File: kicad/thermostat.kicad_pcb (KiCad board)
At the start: 2 copper layers, 108 x 80 mm, 27 parts, among them IC1 LM2596S-5, J1 Display i2c, J2 Sensor i2c, J6 Screw_Terminal_01x05

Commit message: Updates for v1.1
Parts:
- L1: footprint Inductors_SMD:L_Wuerth_WE-PD-Typ-LS -> Inductors_SMD:L_Wuerth_WE-PD-Typ-M-Typ-S
- moved L1 3.50 mm to (167.8, 163.5)
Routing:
- net Net-(D2-Pad1): track 57.7 -> 55.9 mm

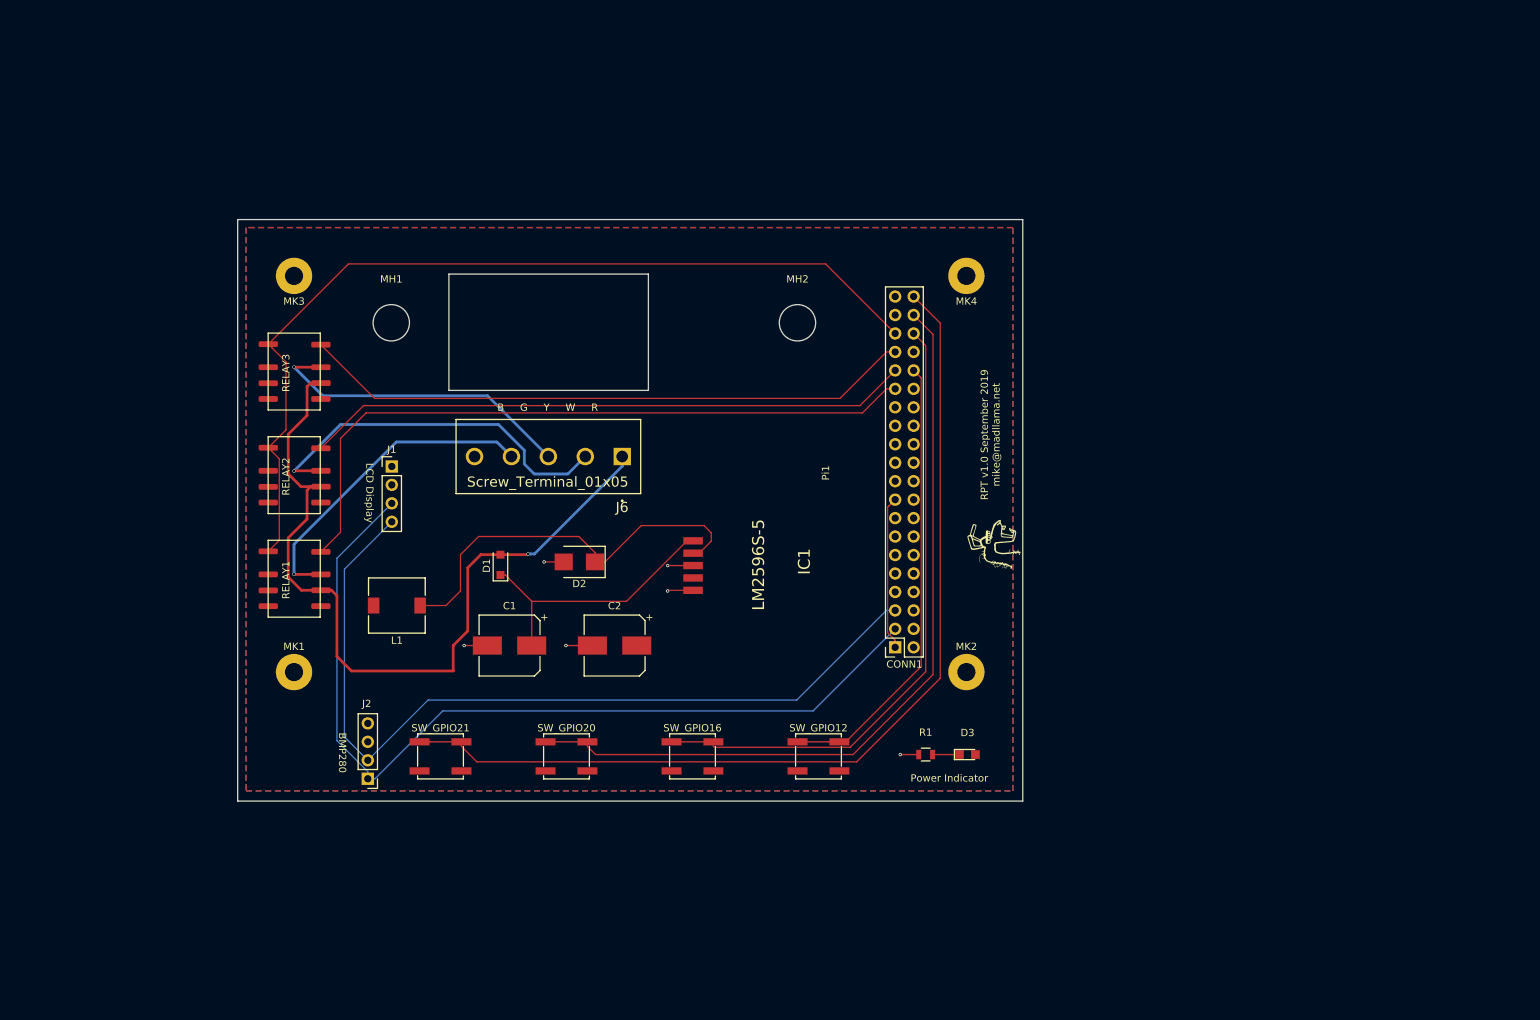
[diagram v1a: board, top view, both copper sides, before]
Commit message: Support for KiCad v5.14 libraries
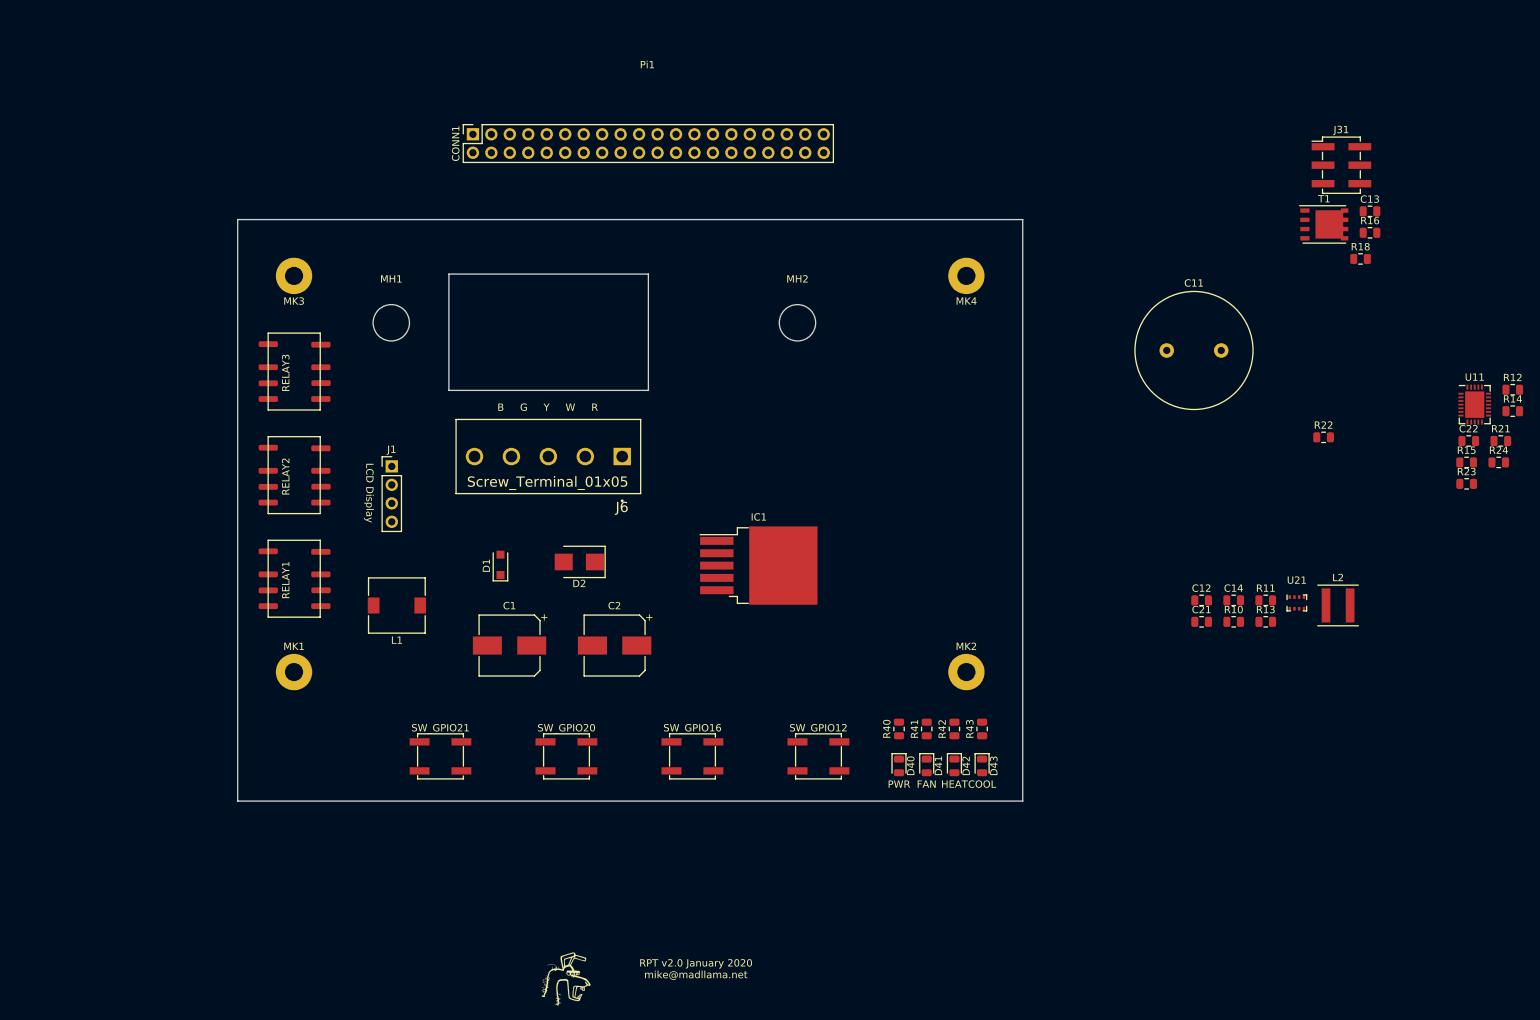
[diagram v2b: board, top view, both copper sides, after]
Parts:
- removed J2: Sensor i2c, Socket_Strips:Socket_Strip_Straight_1x04_Pitch2.54mm
- added C11: 25F, Capacitor_THT:C_Radial_D16.0mm_H31.5mm_P7.50mm, F.Cu at (273.7, 128.4)
- added C12: 2.2uF, Capacitor_SMD:C_0805_2012Metric, F.Cu at (278.5, 162.8)
- added C13: 100uF, Capacitor_SMD:C_0805_2012Metric, F.Cu at (301.6, 109.3)
- added C14: 1nF, Capacitor_SMD:C_0805_2012Metric, F.Cu at (282.9, 162.8)
- added C21: 1uF, Capacitor_SMD:C_0805_2012Metric, F.Cu at (278.5, 165.7)
- added C22: 100nF, Capacitor_SMD:C_0805_2012Metric, F.Cu at (315.2, 140.9)
- added D41: LED, LED_SMD:LED_0805_2012Metric, F.Cu at (240.6, 185.6)
- added D42: LED, LED_SMD:LED_0805_2012Metric, F.Cu at (244.4, 185.6)
- added D43: LED, LED_SMD:LED_0805_2012Metric, F.Cu at (248.3, 185.6)
- added J31: Conn_02x03_Odd_Even, Connector_PinHeader_2.54mm:PinHeader_2x03_P2.54mm_Vertical_SMD, F.Cu at (297.7, 102.9)
- added L2: 2.2uH, Inductor_SMD:L_Coilcraft_XAL5030, F.Cu at (297.2, 163.5)
- added R10: 113k, Resistor_SMD:R_0805_2012Metric, F.Cu at (282.9, 165.7)
- added R11: 38.3k, Resistor_SMD:R_0805_2012Metric, F.Cu at (287.3, 162.8)
- added R12: 1k, Resistor_SMD:R_0805_2012Metric, F.Cu at (321.3, 133.8)
- added R13: 348k, Resistor_SMD:R_0805_2012Metric, F.Cu at (287.3, 165.7)
- added R14: 698k, Resistor_SMD:R_0805_2012Metric, F.Cu at (321.3, 136.8)
- added R15: 1050k, Resistor_SMD:R_0805_2012Metric, F.Cu at (314.9, 143.8)
- added R16: 200k, Resistor_SMD:R_0805_2012Metric, F.Cu at (301.6, 112.2)
- added R18: 12m, Resistor_SMD:R_0805_2012Metric, F.Cu at (300.3, 115.8)
- added R21: 10k, Resistor_SMD:R_0805_2012Metric, F.Cu at (319.6, 140.9)
- added R22: 10k, Resistor_SMD:R_0805_2012Metric, F.Cu at (295.2, 140.4)
- added R23: 10k, Resistor_SMD:R_0805_2012Metric, F.Cu at (314.9, 146.8)
- added R24: 10k, Resistor_SMD:R_0805_2012Metric, F.Cu at (319.3, 143.8)
- added R41: 1k, Resistor_SMD:R_0805_2012Metric, F.Cu at (240.6, 180.5)
- added R42: 1k, Resistor_SMD:R_0805_2012Metric, F.Cu at (244.4, 180.5)
- added R43: 1k, Resistor_SMD:R_0805_2012Metric, F.Cu at (248.3, 180.5)
- added T1: SIR424DP, Package_SO:PowerPAK_SO-8_Single, F.Cu at (295.3, 111.1)
- added U11: LTC4041, project_footprints:ltc4041, F.Cu at (316.0, 135.9)
- added U21: BMP280, Package_LGA:Bosch_LGA-8_2x2.5mm_P0.65mm_ClockwisePinNumbering, F.Cu at (291.6, 163.1)
- D40: renamed from D3; footprint LEDs:LED_0805 -> LED_SMD:LED_0805_2012Metric
- IC1: footprint project_footprints:TO170P1435X465-6N -> Package_TO_SOT_SMD:TO-263-5_TabPin3
- R40: renamed from R1; footprint Resistors_SMD:R_0805 -> Resistor_SMD:R_0805_2012Metric
- moved CONN1 91.4 mm to (178.2, 98.7), turned to 90 degrees
- moved Gr1 83.8 mm to (191.1, 214.8), turned to 0 degrees
- moved Pi1 61.5 mm to (202.2, 88.6), turned to 0 degrees
- moved D40 9.55 mm to (236.8, 185.6), turned to 270 degrees
- moved R40 5.09 mm to (236.8, 180.5), turned to 90 degrees
- turned IC1 to 0 degrees
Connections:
- net /GND renamed GND
- C2 pad 1: /PWR_5V -> /PWR_5V_RAW
- CONN1 pad 11: (no net) -> /GPIO17(GEN0)
- CONN1 pad 13: (no net) -> /GPIO27(GEN2)
- CONN1 pad 15: (no net) -> /GPIO22(GEN3)
- CONN1 pad 35: /GPIO19(SPI1_MISO) -> (no net)
- IC1 pad 4: /PWR_5V -> /PWR_5V_RAW
- L1 pad 2: /PWR_5V -> /PWR_5V_RAW
- RELAY1 pad 1: /GPIO19(SPI1_MISO) -> /GPIO17(GEN0)
- RELAY1 pad 2: (no net) -> /IND_FAN
- RELAY1 pad 3: (no net) -> /PWR_5V
- RELAY2 pad 1: /GPIO19(SPI1_MISO) -> /GPIO27(GEN2)
- RELAY2 pad 2: (no net) -> /IND_HEAT
- RELAY2 pad 3: (no net) -> /PWR_5V
- RELAY3 pad 1: /GPIO19(SPI1_MISO) -> /GPIO22(GEN3)
- RELAY3 pad 2: (no net) -> /IND_COOL
- RELAY3 pad 3: (no net) -> /PWR_5V
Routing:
- net /GPIO21(SPI1_SCK): track 131.9 -> 0.00 mm
- net /GPIO19(SPI1_MISO): track 126.6 -> 0.00 mm
- net /GPIO2(SDA1): track 123.9 -> 0.00 mm
- net /GPIO3(SCL1): track 117.9 -> 0.00 mm
- net /HVAC_PWR(RED): track 111.9 -> 0.00 mm, vias 1 -> 0
- net /GPIO20(SPI1_MOSI): track 109.5 -> 0.00 mm
- net /GPIO5: track 95.9 -> 0.00 mm
- net /GPIO16: track 87.2 -> 0.00 mm
- net /GPIO13(PWM1): track 84.7 -> 0.00 mm
- net /GPIO6: track 83.4 -> 0.00 mm
- net /GPIO12(PWM0): track 62.5 -> 0.00 mm
- net Net-(D2-Pad1): track 55.9 -> 0.00 mm
- net /HVAC_HEAT(WHITE): track 51.3 -> 0.00 mm, vias 1 -> 0
- net /HVAC_FAN(GREEN): track 44.4 -> 0.00 mm, vias 1 -> 0
- net /HVAC_COOL(YELLOW): track 43.8 -> 0.00 mm, vias 1 -> 0
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- removed copper zone on F.Cu, net /PWR_5V
- removed copper zone on B.Cu, net GND
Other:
- board text added: "COOL"
- board text added: "FAN"
- board text added: "HEAT"
- board text added: "PWR"
- board text added: "RPT v2.0 January 2020 mike@madllama.net"
- board text removed: "BMP280"
- board text removed: "Power Indicator"
- board text removed: "RPT v1.0 September 2019 mike@madllama.net"

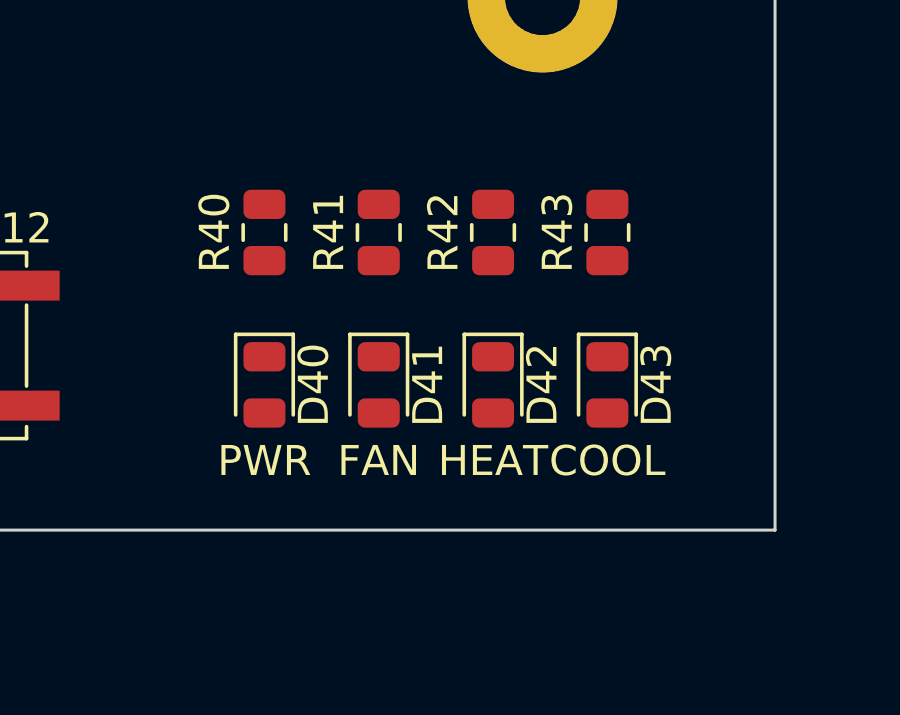
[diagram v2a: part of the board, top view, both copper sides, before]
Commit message: Updated ALL references to new library
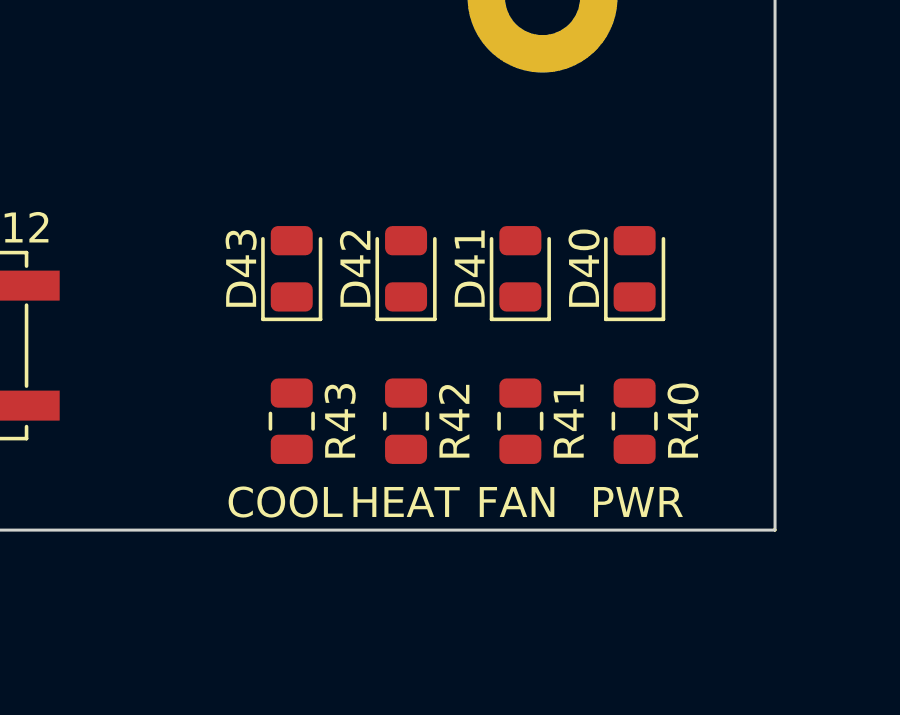
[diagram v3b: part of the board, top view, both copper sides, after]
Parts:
- moved R40 13.9 mm to (249.2, 186.8), turned to 270 degrees
- moved D40 12.9 mm to (249.2, 181.7), turned to 90 degrees
- moved R43 12.3 mm to (237.7, 186.8), turned to 270 degrees
- moved D43 11.2 mm to (237.7, 181.7), turned to 90 degrees
- moved R41 7.86 mm to (245.4, 186.8), turned to 270 degrees
- moved R42 6.93 mm to (241.6, 186.8), turned to 270 degrees
- moved D41 6.10 mm to (245.4, 181.7), turned to 90 degrees
- moved D42 4.84 mm to (241.6, 181.7), turned to 90 degrees

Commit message: ready to start routing
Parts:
- removed J31: Conn_02x03_Odd_Even, Connector_PinHeader_2.54mm:PinHeader_2x03_P2.54mm_Vertical_SMD
- added D44: LED, LED_SMD:LED_0805_2012Metric, F.Cu at (245.7, 185.8)
- added D45: LED, LED_SMD:LED_0805_2012Metric, F.Cu at (242.2, 185.8)
- added D46: LED, LED_SMD:LED_0805_2012Metric, F.Cu at (238.8, 185.8)
- added D47: LED, LED_SMD:LED_0805_2012Metric, F.Cu at (233.9, 185.8)
- added R44: 1k, Resistor_SMD:R_0805_2012Metric, F.Cu at (245.7, 181.5)
- added R45: 1k, Resistor_SMD:R_0805_2012Metric, F.Cu at (242.2, 181.5)
- added R46: 1k, Resistor_SMD:R_0805_2012Metric, F.Cu at (238.8, 181.5)
- added R47: 1k, Resistor_SMD:R_0805_2012Metric, F.Cu at (233.9, 181.5)
- C1, C2: footprint Capacitors_SMD:CP_Elec_8x10 -> Capacitor_SMD:C_Elec_8x10.2
- C11: footprint Capacitor_THT:C_Radial_D16.0mm_H31.5mm_P7.50mm -> Capacitor_THT:CP_Radial_D18.0mm_P7.50mm
- CONN1: footprint Socket_Strips:Socket_Strip_Straight_2x20_Pitch2.54mm -> Connector_PinSocket_2.54mm:PinSocket_2x20_P2.54mm_Vertical
- D1: footprint Diodes_SMD:D_SOD-123F -> Diode_SMD:D_SOD-123F
- D2: footprint Diodes_SMD:D_SMB -> Diode_SMD:D_SMB
- J1: footprint Pin_Headers:Pin_Header_Straight_1x04_Pitch2.54mm -> Connector_PinSocket_2.54mm:PinSocket_1x04_P2.54mm_Vertical
- L1: footprint Inductors_SMD:L_Wuerth_WE-PD-Typ-M-Typ-S -> Inductor_SMD:L_Wuerth_WE-PD-Typ-M-Typ-S
- MH1, MH2: footprint Mounting_Holes:MountingHole_5mm -> MountingHole:MountingHole_5mm
- MK1, MK2, MK3, MK4: footprint Mounting_Holes:MountingHole_2.5mm_Pad -> MountingHole:MountingHole_2.5mm
- R13: value 348k -> 294k
- SW_GPIO12, SW_GPIO16, SW_GPIO20, SW_GPIO21: footprint Buttons_Switches_SMD:SW_SPST_EVPBF -> Button_Switch_SMD:SW_SPST_EVPBF
- T1: footprint Package_SO:PowerPAK_SO-8_Single -> Package_SO:Vishay_PowerPAK_1212-8_Dual
- moved R21 175.6 mm to (149.8, 185.6), turned to 90 degrees
- moved R24 163.3 mm to (160.2, 180.4), turned to 270 degrees
- moved R23 161.6 mm to (156.8, 180.3), turned to 270 degrees
- moved C22 160.4 mm to (161.2, 185.6), turned to 270 degrees
- moved R22 147.2 mm to (153.6, 180.4), turned to 270 degrees
- moved U21 139.4 mm to (153.9, 185.7)
- moved C21 122.3 mm to (157.8, 185.6), turned to 270 degrees
- moved Gr1 98.0 mm to (179.6, 117.5)
- moved R16 84.7 mm to (234.2, 163.4), turned to 90 degrees
- moved R12 83.5 mm to (238.8, 146.6), turned to 90 degrees
- moved RELAY1 82.8 mm to (234.8, 173.0), turned to 0 degrees
- moved R15 82.1 mm to (234.2, 158.9), turned to 90 degrees
- moved U11 77.3 mm to (240.6, 152.6), turned to 270 degrees
- moved R14 76.8 mm to (247.6, 158.5), turned to 270 degrees
- moved T1 74.6 mm to (233.5, 152.7), turned to 180 degrees
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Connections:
- C12 pad 1: /PWR_5V_CAP_IN -> /PWR_5V_RAW
- C13 pad 1: /PWR_5V_CAP -> /PWR_5V
- R10 pad 1: /PWR_5V_CAP_IN -> /PWR_5V_RAW
- R15 pad 2: /PWR_5V_CAP -> /PWR_5V
- R18 pad 2: /PWR_5V_CAP_IN -> /PWR_5V_RAW
- T1 pad 5: /PWR_5V_CAP -> /PWR_5V
- U11 pad 1: /PWR_5V_CAP -> /PWR_5V
- U11 pad 11: (no net) -> /SYSGD
- U11 pad 13: (no net) -> /CAPGD
- U11 pad 14: (no net) -> /PFO
- U11 pad 16: /PWR_5V_CAP_IN -> /PWR_5V_RAW
- U11 pad 24: /PWR_5V_CAP -> /PWR_5V
- U11 pad 6: /PWR_5V_CAP_IN -> /PWR_5V_RAW
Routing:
- net Net-(C11-Pad1): track 0.00 -> 36.3 mm
- net /PWR_5V_RAW: track 0.00 -> 33.7 mm
- net Net-(R15-Pad1): track 0.00 -> 20.0 mm
- net Net-(R10-Pad2): track 0.00 -> 14.1 mm
- net Net-(D2-Pad1): track 0.00 -> 13.7 mm
- net Net-(R18-Pad1): track 0.00 -> 13.4 mm
- net /PWR_5V: track 0.00 -> 13.0 mm
- net Net-(L2-Pad2): track 0.00 -> 7.86 mm
- net Net-(R12-Pad1): track 0.00 -> 4.45 mm
- net Net-(C14-Pad1): track 0.00 -> 4.02 mm
- net Net-(R13-Pad1): track 0.00 -> 2.62 mm
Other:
- outline, holes or cut-outs redrawn
- net class Default: trace_width 0.127 -> 0.254
- net class Power: clearance 0.381 -> 0.127; trace_width 0.381 -> 0.254; via_drill 0.381 -> 0.254
- board text added: "BKUP"
- board text added: "CAP"
- board text added: "PFO"
- board text added: "RAW"
- board text added: "Relay Status"
- board text added: "SYS"
- board text removed: "PWR"

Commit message: almost routed
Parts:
- T1: footprint Package_SO:Vishay_PowerPAK_1212-8_Dual -> Package_SO:Vishay_PowerPAK_1212-8_Single
- moved L1 81.6 mm to (235.9, 172.4), turned to 0 degrees
- moved D46 79.5 mm to (205.2, 113.8), turned to 90 degrees
- moved D45 79.4 mm to (208.8, 113.8), turned to 90 degrees
- moved D44 79.3 mm to (212.5, 113.8), turned to 90 degrees
- moved C2 79.0 mm to (242.7, 160.2), turned to 90 degrees
- moved RELAY1 78.6 mm to (156.8, 163.4), turned to 270 degrees
- moved RELAY2 75.7 mm to (156.8, 135.2), turned to 270 degrees
- moved D2 73.3 mm to (225.8, 172.4), turned to 0 degrees
- moved R46 72.0 mm to (205.3, 117.8), turned to 270 degrees
- moved R45 71.9 mm to (208.8, 117.8), turned to 270 degrees
- moved R44 71.8 mm to (212.5, 117.8), turned to 270 degrees
- moved R11 71.0 mm to (192.1, 113.8), turned to 90 degrees
- moved R42 70.8 mm to (148.9, 132.7)
- moved D42 70.8 mm to (149.0, 137.0)
- moved C14 70.3 mm to (188.5, 113.8), turned to 90 degrees
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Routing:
- net /PWR_5V_RAW: track 33.7 -> 177.7 mm, vias 0 -> 2
- net /GPIO21(SPI1_SCK): track 0.00 -> 123.7 mm
- net /GPIO20(SPI1_MOSI): track 0.00 -> 106.0 mm
- net /PWR_5V: track 13.0 -> 110.5 mm, vias 0 -> 14
- net /GPIO16: track 0.00 -> 88.2 mm
- net /GPIO2(SDA1): track 0.00 -> 82.3 mm
- net /GPIO3(SCL1): track 0.00 -> 74.8 mm
- net /GPIO5: track 0.00 -> 59.0 mm
- net /GPIO12(PWM0): track 0.00 -> 57.8 mm
- net /GPIO6: track 0.00 -> 55.1 mm
- net Net-(C11-Pad1): track 36.3 -> 79.7 mm
- net /GPIO27(GEN2): track 0.00 -> 39.5 mm
- net /GPIO22(GEN3): track 0.00 -> 39.4 mm
- net Net-(T1-Pad4): track 0.00 -> 33.5 mm, vias 0 -> 2
- net Net-(R10-Pad2): track 14.1 -> 39.2 mm
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- added copper zone on B.Cu, net /PWR_5V
- added copper zone on F.Cu, net GND
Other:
- outline, holes or cut-outs redrawn
- board text removed: "LCD Display"
- board text removed: "Relay Status"

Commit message: fully routed v2.0
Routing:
- net /HVAC_PWR(RED): track 0.00 -> 127.5 mm, vias 0 -> 2
- net /HVAC_HEAT(WHITE): track 0.00 -> 113.5 mm, vias 0 -> 1
- net /PWR_3.3V: track 23.9 -> 127.0 mm, vias 0 -> 2
- net /HVAC_COOL(YELLOW): track 0.00 -> 86.2 mm, vias 0 -> 1
- net /GPIO17(GEN0): track 0.00 -> 70.1 mm, vias 0 -> 2
- net /GPIO13(PWM1): track 0.00 -> 59.2 mm, vias 0 -> 2
- net /HVAC_FAN(GREEN): track 0.00 -> 53.8 mm, vias 0 -> 1
- net /GPIO5: track 59.0 -> 61.1 mm
- net Net-(R21-Pad1): track 5.80 -> 7.25 mm
